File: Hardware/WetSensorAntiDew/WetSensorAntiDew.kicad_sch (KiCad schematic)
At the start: 29 parts, among them J1 Teensy Connector, J2 Connector to BME280, J3 1-4 to HeatedWetSensor | 5-7 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, J4 Teensy Connector, J5 Connector to power supply, J6 Connector to power supply, J8 6P6C, Q1 MOSFET N-CH, SW1 SW_Push, U1 AMS1117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

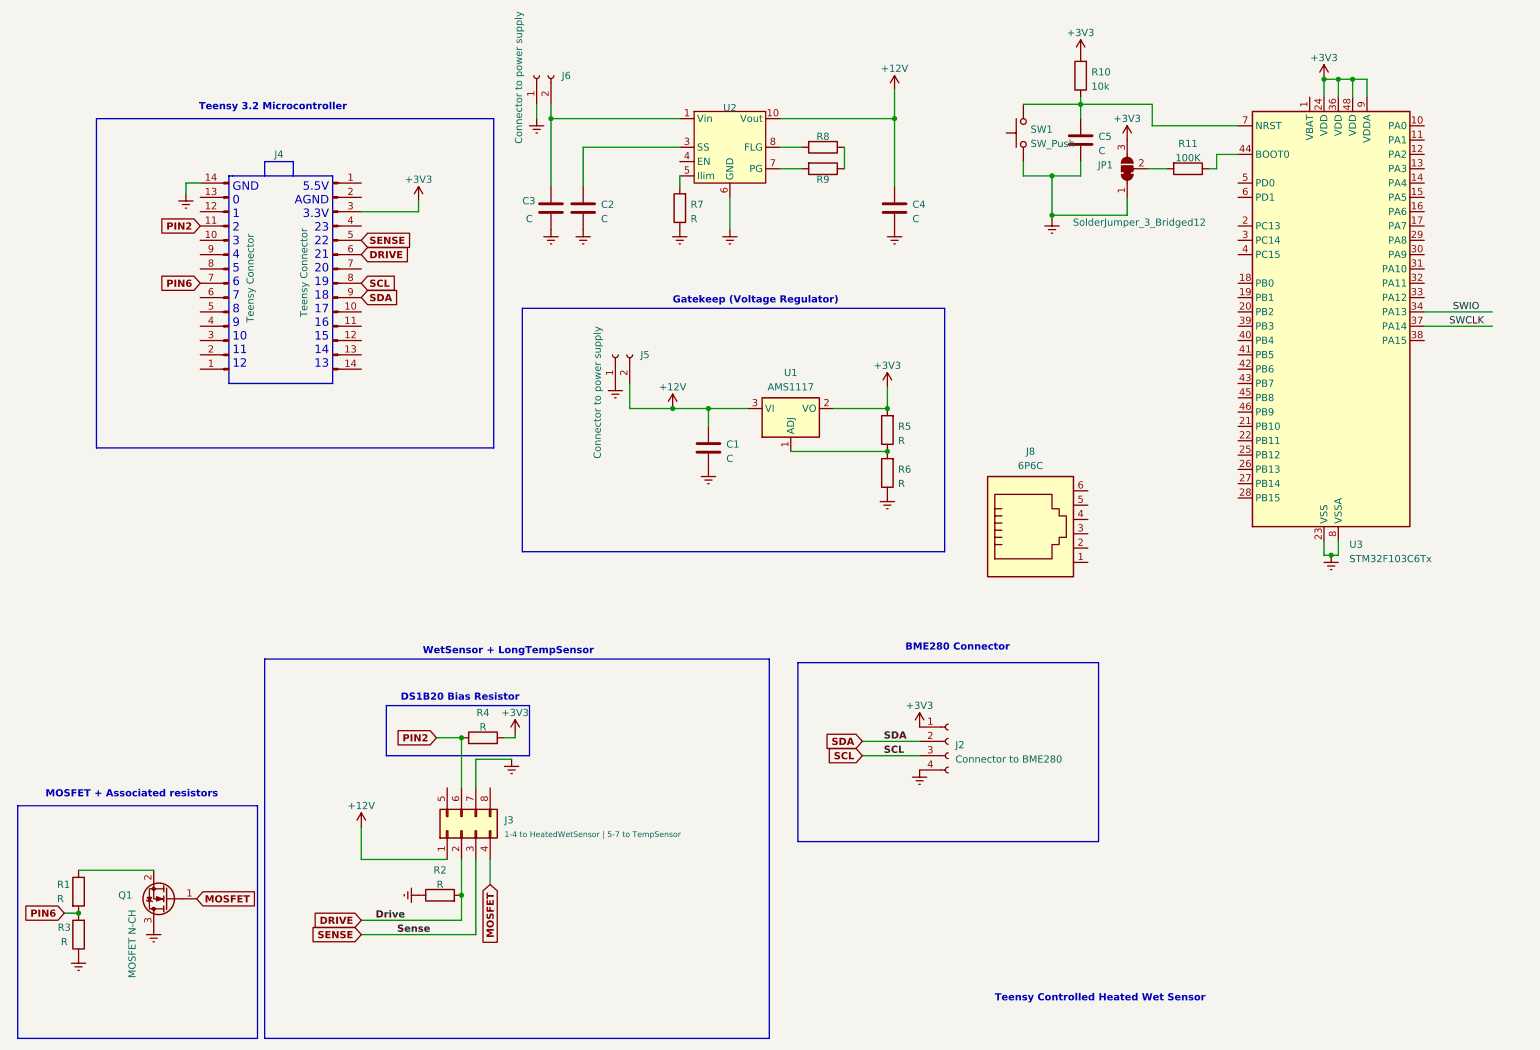
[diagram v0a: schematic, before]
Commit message: added custom stm32 core
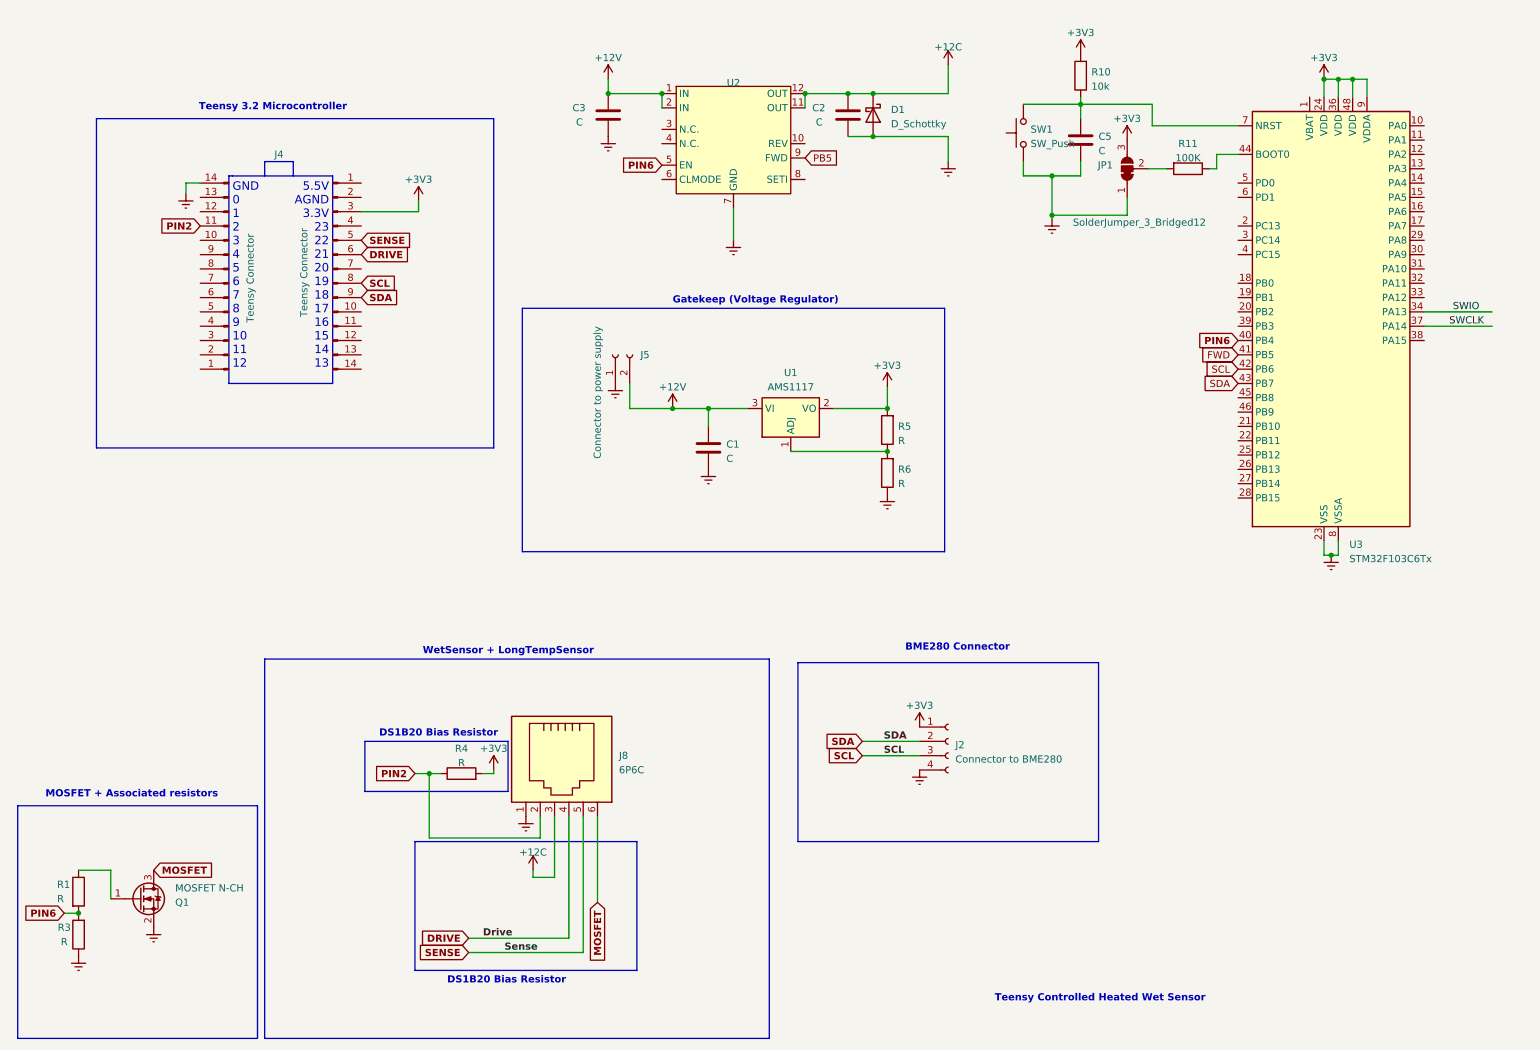
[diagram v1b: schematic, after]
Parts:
- removed C4: C, Capacitor_SMD:C_0603_1608Metric_Pad1.08x0.95mm_HandSolder, symbol Device:C
- removed J3: 1-4 to HeatedWetSensor | 5-7 to TempSensor, Connector_IDC:IDC-Header_2x04_P2.54mm_Horizontal, symbol Connector_Generic:Conn_02x04_Top_Bottom
- removed J6: Connector to power supply, Connector_Phoenix_MSTB:PhoenixContact_MSTBA_2,5_2-G_1x02_P5.00mm_Horizontal, symbol Connector:Conn_01x02_Socket
- removed R2, R7, R8, R9: R, Resistor_SMD:R_0603_1608Metric_Pad0.98x0.95mm_HandSolder, symbol Device:R
- removed U2: ~, symbol AntiDew_Library:SiP32430
- added D1: D_Schottky, symbol Device:D_Schottky
- added U2: ~, symbol AntiDew_Library:MAX17610
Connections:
- net +12V: now also C3.1, U2.1 (IN), U2.2 (IN)
- net DRIVE: now also J8.4
- net Earth: now also J8.1, Q1.2 (S), D1.2 (A), U2.7 (GND); no longer Q1.3 (D)
- net MOSFET: now also J8.6, Q1.3 (D); no longer Q1.1 (G)
- net PIN2: now also J8.2
- net PIN6: now also U3.40 (PB4), U2.5 (EN); no longer J1.7 (Pin_7)
- net SCL: now also U3.42 (PB6)
- net SDA: now also U3.43 (PB7)
- net SENSE: now also J8.5
- net FWD: now reaches U3.41 (PB5)
- net +12C: now reaches C2.1
- net +12C: now also J8.3, D1.1 (K), U2.11 (OUT), U2.12 (OUT)
- net at R1.1: now also Q1.1 (G); no longer Q1.2 (S)
- new net PB5: U2.9 (FWD)
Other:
- moved on the sheet: C3, J8, R4

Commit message: Updates to board
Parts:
- added C4, C6: C, Capacitor_SMD:C_0603_1608Metric_Pad1.08x0.95mm_HandSolder, symbol Device:C_Small
- added J3: 4P4C, footprints:BEL_SS-6444-NF, symbol Connector:4P4C
- added R2: R, Resistor_SMD:R_0603_1608Metric_Pad0.98x0.95mm_HandSolder, symbol Device:R
- added Y1: Crystal_GND24_Small, symbol Device:Crystal_GND24_Small
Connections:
- net Earth: now also Y1.2, Y1.4
- net Boot: now reaches R11.1, U3.44 (BOOT0)
- net OSCIN: now reaches U3.5 (PD0)
- net OSCIN: now also C4.1, R2.1, Y1.3
- net OSCOUT: now reaches U3.6 (PD1)
- net OSCOUT: now also C6.1, R2.2, Y1.1
- new net: C4.2, C6.2
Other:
- note added: "Core Oscillator"

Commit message: More progress
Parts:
- removed J1, J4: Teensy Connector, Connector_PinHeader_2.54mm:PinHeader_1x14_P2.54mm_Vertical, symbol Connector:Conn_01x14_Male
- added J6: Conn_01x04_Socket, Connector:FanPinHeader_1x04_P2.54mm_Vertical, symbol Connector:Conn_01x04_Socket
- added JP2, JP3: SolderJumper_2_Open, Jumper:SolderJumper-2_P1.3mm_Open_Pad1.0x1.5mm, symbol Jumper:SolderJumper_2_Open
- added R7: 10k, Resistor_SMD:R_0603_1608Metric_Pad0.98x0.95mm_HandSolder, symbol Device:R
- D1: footprint (none) -> Diode_SMD:D_SOD-323
- J2: symbol Connector:Conn_01x04_Female -> Connector:Conn_01x05_Socket
- SW1: footprint (none) -> footprints:228EJVAYFR
- U2: footprint (none) -> Package_DFN_QFN:DFN-12-1EP_3x3mm_P0.5mm_EP1.6x2.5mm_ThermalVias
- Y1: footprint (none) -> Crystal:Crystal_SMD_3225-4Pin_3.2x2.5mm
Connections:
- net DRIVE is gone; now on net WET2: J8.4
- net SENSE is gone; now on net WET1: J8.5
- net +12C: now also JP2.2 (B)
- net +12V: now also JP2.1 (A)
- net +3V3: now also J6.4 (Pin_4)
- net Earth: now also J2.5 (Pin_5), J6.1 (Pin_1), JP3.1 (A), R7.1; no longer J2.4 (Pin_4)
- net MOSFET: now also JP3.2 (B)
- net SWCLK: now also J6.2 (Pin_2)
- net SWIO: now also J6.3 (Pin_3)
- net PA0: now reaches U3.10 (PA0)
- net PA0: now also U2.8 (SETI), R7.2
- net WET2: now reaches J3.3
- net WET1: now reaches J3.4
- no-connect marks 0 -> 3
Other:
- note added: "Connector to CIMEL"
- note added: "Wet Sensor"
- note removed: "5.5V AGND 3.3V 23 22 21 20 19 18 17 16 15 14 13"
- note removed: "GND 0 1 2 3 4 5 6 7 8 9 10 11 12"
- note removed: "Teensy 3.2 Microcontroller"
- moved on the sheet: J3

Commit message: finished pcb layout
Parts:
- removed JP1: SolderJumper_3_Bridged12, Jumper:SolderJumper-3_P1.3mm_Bridged12_Pad1.0x1.5mm_NumberLabels, symbol Jumper:SolderJumper_3_Bridged12
- added C7: C, Capacitor_SMD:C_0603_1608Metric_Pad1.08x0.95mm_HandSolder, symbol Device:C
- J2: footprint Connector_PinSocket_2.54mm:PinSocket_1x04_P2.54mm_Horizontal -> Connector_PinSocket_2.54mm:PinSocket_1x05_P2.54mm_Horizontal
- J5: footprint Connector_Phoenix_MSTB:PhoenixContact_MSTBA_2,5_2-G_1x02_P5.00mm_Horizontal -> Connector_Phoenix_MC:PhoenixContact_MC_1,5_2-G-3.81_1x02_P3.81mm_Horizontal
- R7: value 10k -> 1.5k
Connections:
- net +3V3: now also C7.1
- net Earth: now also R11.2, U2.13 (GND), U2.6 (CLMODE)
- net PA0: now also U3.29 (PA8); no longer U3.10 (PA0)
- net PB5: now also U3.32 (PA11)
- net PIN6: now also U3.31 (PA10)
- net at R5.1, R6.2, U1.1 (ADJ): now also C7.2
- net FWD: no longer names the net of U3.41 (PB5)
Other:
- note added: "CLMODE low continuous mode"
- note added: "sets 1 amp current limit"
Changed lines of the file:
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@@
   (junction (at 247.015 111.125) (diameter 0) (color 0 0 0 0)
   )
+  (junction (at 140.97 49.53) (diameter 0) (color 0 0 0 0)
+  )
+  (junction (at 163.83 85.09) (diameter 0) (color 0 0 0 0)
+  )
   (junction (at 165.735 36.83) (diameter 0) (color 0 0 0 0)
   )
@@
   )
   (junction (at 161.29 29.21) (diameter 0) (color 0 0 0 0)
+  )
+  (junction (at 163.83 92.71) (diameter 0) (color 0 0 0 0)
   )
   (junction (at 165.735 29.21) (diameter 0) (color 0 0 0 0)
@@
     (stroke (width 0) (type default))
   )
+  (wire (pts (xy 163.83 85.09) (xy 168.275 85.09))
+    (stroke (width 0) (type default))
+  )
   (wire (pts (xy 161.29 36.83) (xy 165.735 36.83))
     (stroke (width 0) (type default))
@@
     (stroke (width 0) (type default))
   )
-  (wire (pts (xy 214.63 42.545) (xy 217.805 42.545))
-    (stroke (width 0) (type default))
-  )
   (wire (pts (xy 165.735 29.21) (xy 172.085 29.21))
     (stroke (width 0) (type default))
@@
     (stroke (width 0) (type default))
   )
-  (wire (pts (xy 158.75 85.09) (xy 168.275 85.09))
+  (wire (pts (xy 217.805 42.545) (xy 210.82 42.545))
     (stroke (width 0) (type default))
   )
@@
     (stroke (width 0) (type default))
   )
+  (wire (pts (xy 163.83 92.71) (xy 168.275 92.71))
+    (stroke (width 0) (type default))
+  )
   (wire (pts (xy 93.98 179.07) (xy 111.76 179.07))
     (stroke (width 0) (type default))
@@
     (stroke (width 0) (type default))
   )
-  (wire (pts (xy 210.82 47.625) (xy 210.82 50.8))
+  (wire (pts (xy 210.82 42.545) (xy 210.82 50.8))
     (stroke (width 0) (type default))
   )
@@
     (stroke (width 0) (type default))
   )
+  (wire (pts (xy 151.13 92.71) (xy 163.83 92.71))
+    (stroke (width 0) (type default))
+  )
   (wire (pts (xy 122.555 80.645) (xy 122.555 85.09))
     (stroke (width 0) (type default))
@@
     (stroke (width 0) (type default))
   )
-  (wire (pts (xy 151.13 92.71) (xy 168.275 92.71))
-    (stroke (width 0) (type default))
-  )
   (wire (pts (xy 245.745 111.125) (xy 247.015 111.125))
     (stroke (width 0) (type default))
@@
     (stroke (width 0) (type default))
   )
+  (wire (pts (xy 140.97 49.53) (xy 143.51 49.53))
+    (stroke (width 0) (type default))
+  )
   (wire (pts (xy 42.545 177.165) (xy 42.545 175.895))
     (stroke (width 0) (type default))
   )
   (wire (pts (xy 201.295 84.455) (xy 213.36 84.455))
+    (stroke (width 0) (type default))
+  )
+  (wire (pts (xy 158.75 85.09) (xy 163.83 85.09))
     (stroke (width 0) (type default))
   )
@@
     (effects (font (size 1.27 1.27) bold) (justify left bottom))
   )
+  (text "CLMODE low continuous mode" (at 102.87 50.165 0)
+    (effects (font (size 1.27 1.27)) (justify left bottom))
+  )
   (text "Wet Sensor" (at 90.17 187.325 0)
     (effects (font (size 1.27 1.27) bold) (justify left bottom))
@@
     (effects (font (size 1.27 1.27) (thickness 0.254) bold) (justify left bottom))
   )
+  (text "sets 1 amp current limit\n" (at 160.02 50.165 0)
+    (effects (font (size 1.27 1.27)) (justify left bottom))
+  )
   (text "Core Oscillator\n" (at 242.57 121.285 0)
     (effects (font (size 1.27 1.27)) (justify left bottom))
@@
   (label "SWIO" (at 268.605 67.945 0) (fields_autoplaced)
     (effects (font (size 1.27 1.27)) (justify left bottom))
-  )
-  (global_label "PA0" (shape input) (at 263.525 34.925 0) (fields_autoplaced)
-    (effects (font (size 1.27 1.27)) (justify left))
-    (property "Intersheetrefs" "${INTERSHEET_REFS}" (at 269.9989 34.925 0)
-      (effects (font (size 1.27 1.27)) (justify left) hide)
-    )
   )
   (global_label "OSCIN" (shape input) (at 230.505 45.085 180) (fields_autoplaced)
@@
     )
   )
+  (global_label "PIN6" (shape input) (at 263.525 60.325 0) (fields_autoplaced)
+    (effects (font (size 1.27 1.27) bold) (justify left))
+    (property "Intersheetrefs" "${INTERSHEET_REFS}" (at 271.274 60.325 0)
+      (effects (font (size 1.27 1.27)) (justify left) hide)
+    )
+  )
   (global_label "SCL" (shape input) (at 230.505 78.105 180) (fields_autoplaced)
     (effects (font (size 1.27 1.27)) (justify right))
@@
     )
   )
+  (global_label "PB5" (shape input) (at 263.525 62.865 0) (fields_autoplaced)
+    (effects (font (size 1.27 1.27)) (justify left))
+    (property "Intersheetrefs" "${INTERSHEET_REFS}" (at 270.1803 62.865 0)
+      (effects (font (size 1.27 1.27)) (justify left) hide)
+    )
+  )
   (global_label "OSCIN" (shape input) (at 252.095 135.255 90) (fields_autoplaced)
     (effects (font (size 1.27 1.27)) (justify left))
@@
     )
   )
-  (global_label "FWD" (shape input) (at 230.505 75.565 180) (fields_autoplaced)
-    (effects (font (size 1.27 1.27)) (justify right))
-    (property "Intersheetrefs" "${INTERSHEET_REFS}" (at 223.7892 75.565 0)
-      (effects (font (size 1.27 1.27)) (justify right) hide)
+  (global_label "PA0" (shape input) (at 263.525 55.245 0) (fields_autoplaced)
+    (effects (font (size 1.27 1.27)) (justify left))
+    (property "Intersheetrefs" "${INTERSHEET_REFS}" (at 269.9989 55.245 0)
+      (effects (font (size 1.27 1.27)) (justify left) hide)
     )
   )
@@
       (effects (font (size 1.27 1.27)) (justify right))
     )
-    (property "Value" "10k" (at 155.575 50.165 0)
+    (property "Value" "1.5k" (at 155.575 50.165 0)
       (effects (font (size 1.27 1.27)) (justify right))
     )
@@
       (effects (font (size 1.27 1.27)) (justify left))
     )
-    (property "Footprint" "Connector_PinSocket_2.54mm:PinSocket_1x04_P2.54mm_Horizontal" (at 179.07 144.145 0)
+    (property "Footprint" "Connector_PinSocket_2.54mm:PinSocket_1x05_P2.54mm_Horizontal" (at 179.07 144.145 0)
       (effects (font (size 1.27 1.27)) hide)
     )
@@
     (pin "11")
     (pin "12")
+    (pin "13")
     (pin "2")
     (pin "3")
@@
     )
   )
-  (symbol (lib_id "Jumper:SolderJumper_3_Bridged12") (at 210.82 42.545 90) (unit 1)
-    (in_bom yes) (on_board yes) (dnp no)
-    (property "Reference" "JP1" (at 208.28 41.91 90)
-      (effects (font (size 1.27 1.27)) (justify left))
-    )
-    (property "Value" "SolderJumper_3_Bridged12" (at 224.79 52.07 90)
-      (effects (font (size 1.27 1.27)) (justify left))
-    )
-    (property "Footprint" "Jumper:SolderJumper-3_P1.3mm_Bridged12_Pad1.0x1.5mm_NumberLabels" (at 210.82 42.545 0)
-      (effects (font (size 1.27 1.27)) hide)
-    )
-    (property "Datasheet" "~" (at 210.82 42.545 0)
-      (effects (font (size 1.27 1.27)) hide)
-    )
-    (pin "1")
-    (pin "2")
-    (pin "3")
-    (instances
-      (project "WetSensorAntiDew"
-        (path "/4d9ca3a9-89cf-4a0b-a8ab-770e84bd9292"
-          (reference "JP1") (unit 1)
-        )
-      )
-    )
-  )
   (symbol (lib_id "power:Earth") (at 38.1 177.165 0) (unit 1)
     (in_bom yes) (on_board yes) (dnp no) (fields_autoplaced)
@@
         (path "/4d9ca3a9-89cf-4a0b-a8ab-770e84bd9292"
           (reference "#PWR02") (unit 1)
+        )
+      )
+    )
+  )
+  (symbol (lib_id "power:Earth") (at 128.27 44.45 0) (unit 1)
+    (in_bom yes) (on_board yes) (dnp no) (fields_autoplaced)
+    (property "Reference" "#PWR028" (at 128.27 50.8 0)
+      (effects (font (size 1.27 1.27)) hide)
+    )
+    (property "Value" "Earth" (at 128.27 48.26 0)
+      (effects (font (size 1.27 1.27)) hide)
+    )
+    (property "Footprint" "" (at 128.27 44.45 0)
+      (effects (font (size 1.27 1.27)) hide)
+    )
+    (property "Datasheet" "~" (at 128.27 44.45 0)
+      (effects (font (size 1.27 1.27)) hide)
+    )
+    (pin "1")
+    (instances
+      (project "WetSensorAntiDew"
+        (path "/4d9ca3a9-89cf-4a0b-a8ab-770e84bd9292"
+          (reference "#PWR028") (unit 1)
         )
       )
@@
       (effects (font (size 1.27 1.27)) (justify right))
     )
-    (property "Footprint" "Connector_Phoenix_MSTB:PhoenixContact_MSTBA_2,5_2-G_1x02_P5.00mm_Horizontal" (at 120.015 75.565 0)
+    (property "Footprint" "Connector_Phoenix_MC:PhoenixContact_MC_1,5_2-G-3.81_1x02_P3.81mm_Horizontal" (at 120.015 75.565 0)
       (effects (font (size 1.27 1.27)) hide)
     )
@@
     )
   )
+  (symbol (lib_id "Device:C") (at 163.83 88.9 0) (unit 1)
+    (in_bom yes) (on_board yes) (dnp no)
+    (property "Reference" "C7" (at 157.48 87.63 0)
+      (effects (font (size 1.27 1.27)) (justify left))
+    )
+    (property "Value" "C" (at 158.115 90.17 0)
+      (effects (font (size 1.27 1.27)) (justify left))
+    )
+    (property "Footprint" "Capacitor_SMD:C_0603_1608Metric_Pad1.08x0.95mm_HandSolder" (at 164.7952 92.71 0)
+      (effects (font (size 1.27 1.27)) hide)
+    )
+    (property "Datasheet" "~" (at 163.83 88.9 0)
+      (effects (font (size 1.27 1.27)) hide)
+    )
+    (pin "1")
+    (pin "2")
+    (instances
+      (project "WetSensorAntiDew"
+        (path "/4d9ca3a9-89cf-4a0b-a8ab-770e84bd9292"
+          (reference "C7") (unit 1)
+        )
+      )
+    )
+  )
   (symbol (lib_id "power:+3V3") (at 173.99 139.065 0) (unit 1)
     (in_bom yes) (on_board yes) (dnp no) (fields_autoplaced)
@@
         )
       )
-    )
-  )
-  (symbol (lib_id "power:+3V3") (at 210.82 37.465 0) (unit 1)
-    (in_bom yes) (on_board yes) (dnp no) (fields_autoplaced)
-    (property "Reference" "#PWR026" (at 210.82 41.275 0)
-      (effects (font (size 1.27 1.27)) hide)
-    )
-    (property "Value" "+3V3" (at 210.82 33.655 0)
-      (effects (font (size 1.27 1.27)))
-    )
-    (property "Footprint" "" (at 210.82 37.465 0)
-      (effects (font (size 1.27 1.27)) hide)
-    )
-    (property "Datasheet" "" (at 210.82 37.465 0)
-      (effects (font (size 1.27 1.27)) hide)
-    )
-    (pin "1")
-    (instances
-      (project "WetSensorAntiDew"
-        (path "/4d9ca3a9-89cf-4a0b-a8ab-770e84bd9292"
-          (reference "#PWR026") (unit 1)
-        )
-      )
